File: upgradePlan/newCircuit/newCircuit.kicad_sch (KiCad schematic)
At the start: 14 parts

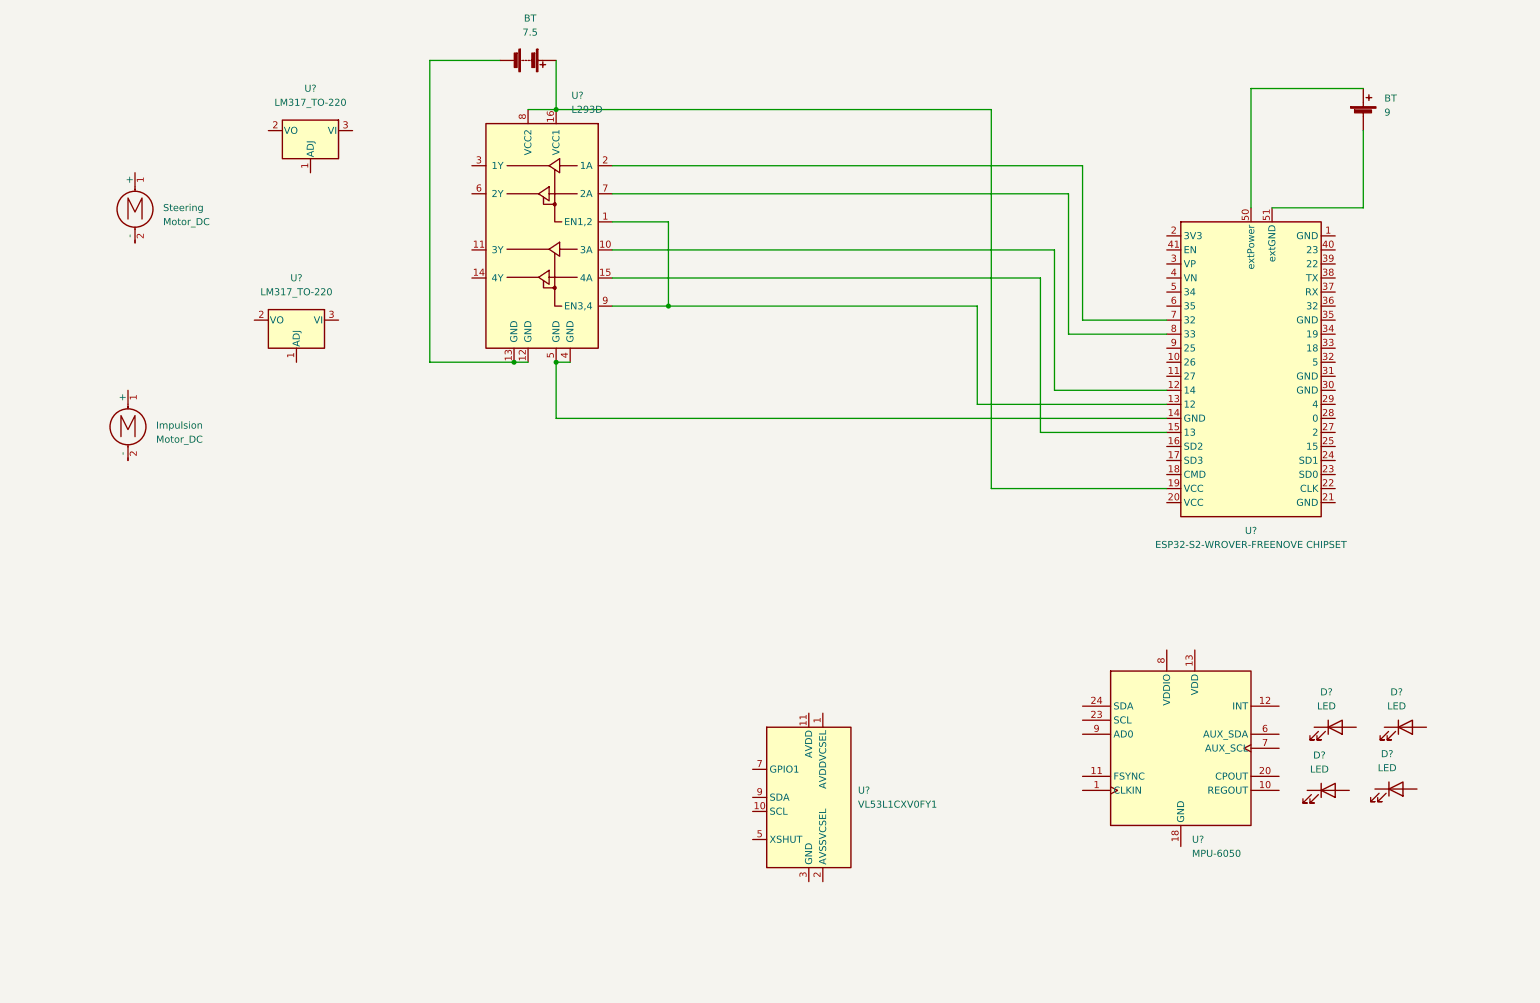
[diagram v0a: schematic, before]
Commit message: motor ciurcuit in kicad partial in picture
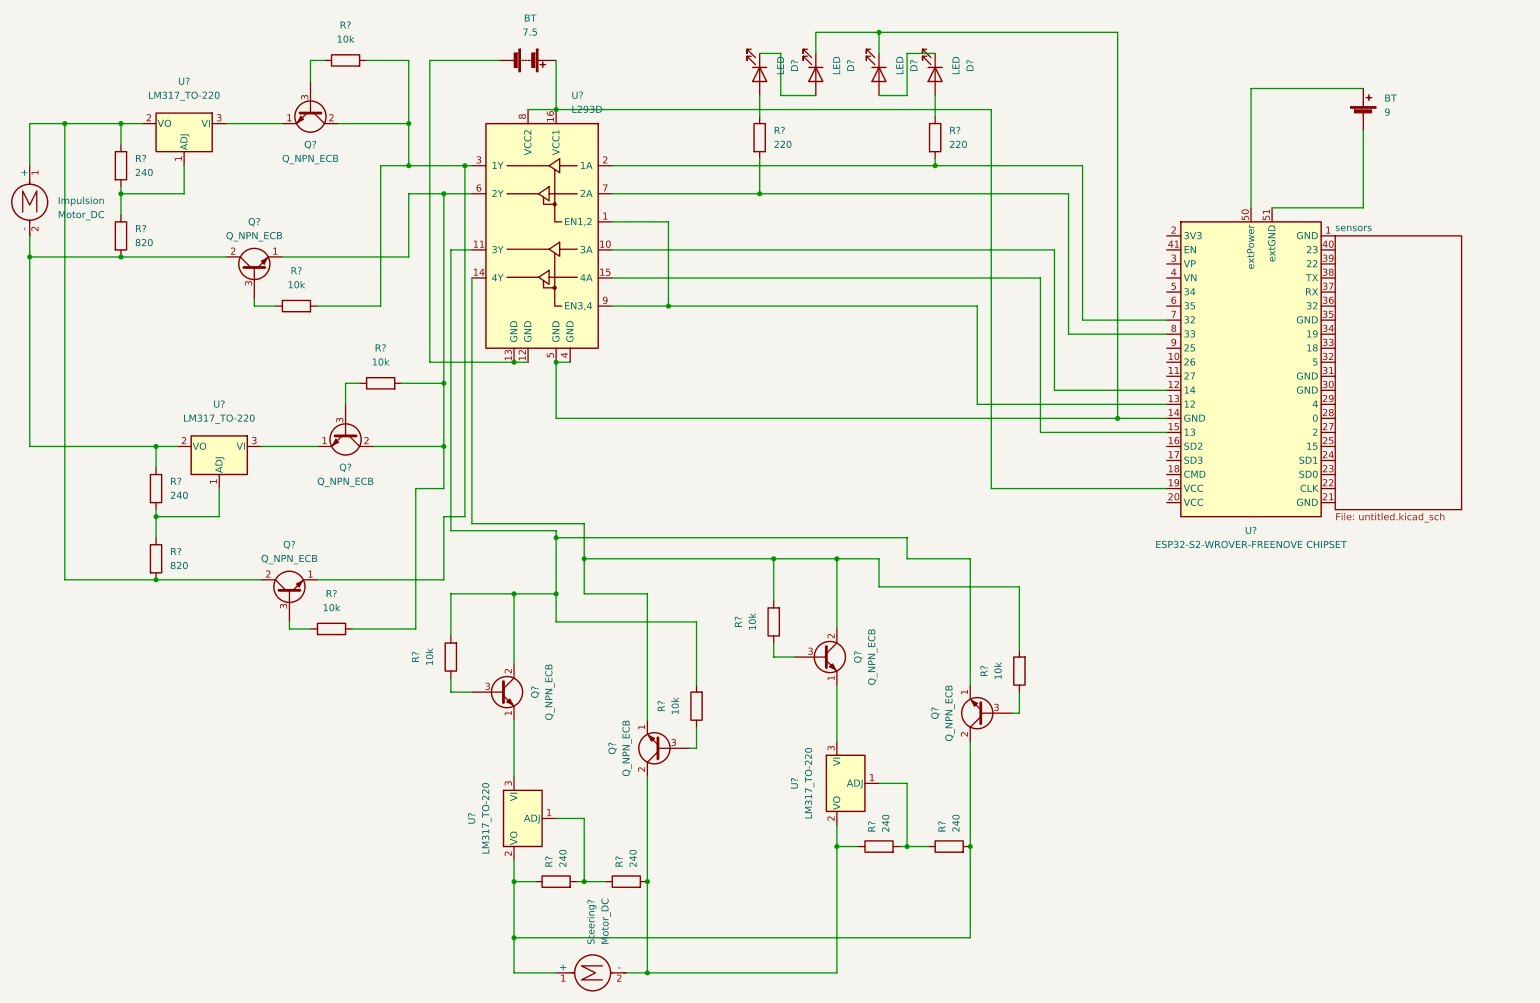
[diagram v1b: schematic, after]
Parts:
- removed D? (x4): LED, symbol Device:LED
- removed Impulsion: Motor_DC, symbol Motor:Motor_DC
- removed U?: MPU-6050, Sensor_Motion:InvenSense_QFN-24_4x4mm_P0.5mm, symbol Sensor_Motion:MPU-6050
- removed U?: LM317_TO-220, Package_TO_SOT_THT:TO-220-3_Vertical, symbol Regulator_Linear:LM317_TO-220
- removed U?: VL53L1CXV0FY1, Sensor_Distance:ST_VL53L1x, symbol Sensor_Distance:VL53L1CXV0FY1
- added D? (x4): LED, symbol Device:LED
- added Q? (x8): Q_NPN_ECB, symbol Device:Q_NPN_ECB
- added R? (x8): 10k, symbol Device:R
- added R? (x6): 240, symbol Device:R
- added R? (x2): 220, symbol Device:R
- added R? (x2): 820, symbol Device:R
- added Steering?: Motor_DC, symbol Motor:Motor_DC
- added U? (x3): LM317_TO-220, Package_TO_SOT_THT:TO-220-3_Vertical, symbol Regulator_Linear:LM317_TO-220
- renumbered Steering to Impulsion
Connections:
- net at U?.1 (ADJ): now also R?.1, R?.2
- net at U?.2 (VO): now also Impulsion.1 (+), Q?.2 (C), R?.1, R?.2
- net at U?.3 (VI): now also Q?.1 (E)
- net at U?.11 (3Y): now also Q?.1 (E), Q?.2 (C), R?.2, R?.2
- net at U?.14 (4Y): now also Q?.1 (E), Q?.2 (C), R?.2, R?.2
- net at U?.2 (1A), U?.7 (32): now also R?.2
- net at U?.3 (1Y): now also Q?.1 (E), Q?.2 (C), R?.2, R?.2
- net at U?.14 (GND), U?.4 (GND), U?.5 (GND): now also D?.1 (K), D?.1 (K)
- net at U?.6 (2Y): now also Q?.1 (E), Q?.2 (C), R?.2, R?.2
- net at U?.7 (2A), U?.8 (33): now also R?.2
- net at Impulsion.2 (-): now also Q?.2 (C), R?.1, R?.2, U?.2 (VO)
- new net: Q?.2 (C), R?.1, R?.2, Steering?.2 (-), U?.2 (VO)
- new net: Q?.3 (B), R?.1 (x8)
- new net: Q?.2 (C), R?.1, R?.2, Steering?.1 (+), U?.2 (VO)
- new net: R?.1, R?.2, U?.1 (ADJ) (x3)
- new net: D?.1 (K), D?.2 (A) (x2)
- new net: Q?.1 (E), U?.3 (VI) (x3)
- new net: D?.2 (A), R?.1 (x2)
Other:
- added sheet sensors (untitled.kicad_sch)
- moved on the sheet: Impulsion, U?

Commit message: circuit V0.1
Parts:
- removed BT: 9, symbol Device:Battery_Cell
- removed BT: 7.5, symbol Device:Battery
- removed D? (x4): LED, symbol Device:LED
- removed Impulsion, Steering?: Motor_DC, symbol Motor:Motor_DC
- removed Q? (x8): Q_NPN_ECB, symbol Device:Q_NPN_ECB
- removed R? (x8): 10k, symbol Device:R
- removed R? (x6): 240, symbol Device:R
- removed R? (x2): 220, symbol Device:R
- removed R? (x2): 820, symbol Device:R
- removed U? (x4): LM317_TO-220, Package_TO_SOT_THT:TO-220-3_Vertical, symbol Regulator_Linear:LM317_TO-220
- removed U?: L293D, Package_DIP:DIP-16_W7.62mm, symbol Driver_Motor:L293D
- removed U?: ESP32-S2-WROVER-FREENOVE CHIPSET, RF_Module:ESP32-S2-WROVER, symbol My_RC_Car:ESP32-S2-WROVER-FREENOVE CHIPSET
- added BT1: Battery_Cell, symbol Device:Battery_Cell
- added C1: 0.1 u, symbol Device:C
- added D1, D2, D3, D4: LED, symbol Device:LED
- added J1: Connector_GY_521, symbol Connector:Connector_GY-521
- added M1: Motor_DC, symbol Motor:Motor_DC
- added M2: Motor_Servo, symbol Motor:Motor_Servo
- added R1, R8: 120, symbol Device:R
- added R2: 510, symbol Device:R
- added R3, R4: 220, symbol Device:R
- added R7: 39, symbol Device:R
- added SW1: SW_DIP_x01, symbol Switch:SW_DIP_x01
- added U1: Freenove-SP32-WROVER, RF_Module:Freenove-ESP32-WROVER, symbol RF_Module:ESP32-S2-WROVER
- added U2: L293D, Package_DIP:DIP-16_W7.62mm, symbol Driver_Motor:L293D
- added U3, U5: LM317_TO-220, Package_TO_SOT_THT:TO-220-3_Vertical, symbol Regulator_Linear:LM317_TO-220
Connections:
- new net: C1.1, M1.1 (+), U2.3 (1Y)
- new net: C1.2, M1.2 (-), U2.6 (2Y)
- new net: M2.1 (PWM), U1.8 (33)
- new net: BT1.1 (+), SW1.1
- new net: SW1.2, U3.3 (VI), U5.3 (VI)
- new net: R1.2, R2.1, U3.1 (ADJ)
- new net: D3.2 (A), D4.1 (K)
- new net: D1.1 (K), D2.2 (A)
- new net: D1.2 (A), R3.2
- new net: J1.1 (VCC), U1.2 (3V3)
- new net: J1.3 (SCL), U1.38 (22)
- new net: J1.4 (SDA), U1.35 (21)
- new net: J1.8 (INT), U1.11 (27)
- new net: D4.2 (A), R4.2
- new net: R4.1, U1.6 (35), U2.7 (2A)
- new net: R7.2, R8.1, U5.1 (ADJ)
- new net: U1.5 (34), U2.1 (EN1,2)
- new net: R3.1, U1.7 (32), U2.2 (1A)
- new net Drive Motor: R1.1, U2.16 (VCC1), U2.8 (VCC2), U3.2 (VO)
- new net ESP Power: M2.2 (+), R7.1, U1.19 (VCC), U5.2 (VO)
- new net GND: BT1.2 (-), D2.1 (K), D3.1 (K), J1.2 (GND), M2.3 (-), R2.2, R8.2, U1.30 (GND), U2.4 (GND)
- no-connect marks 0 -> 23
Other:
- removed sheet sensors
- title: new ciruit rospCar -> (none)
